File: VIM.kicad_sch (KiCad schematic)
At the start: 13 parts, among them U3 INA139, U4 MAX11615, U5 INA139

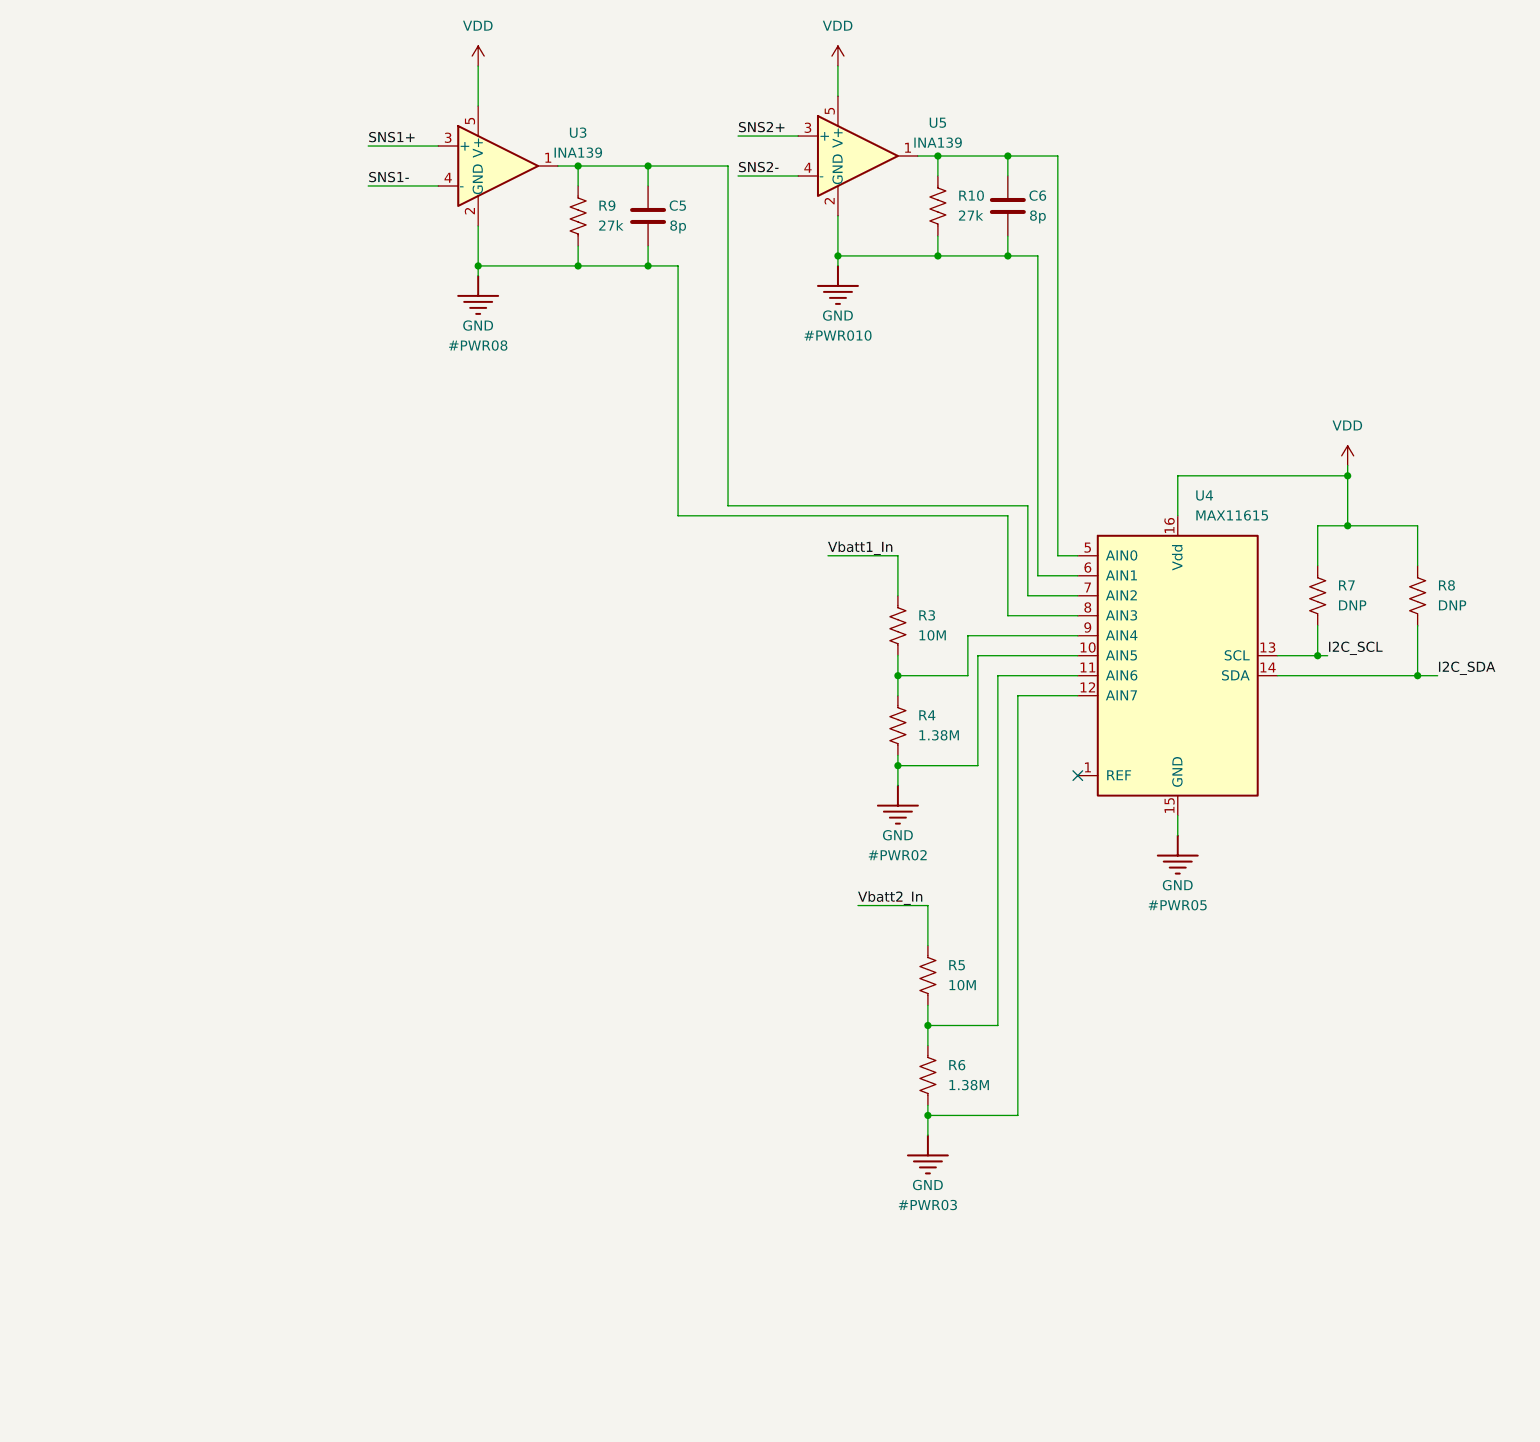
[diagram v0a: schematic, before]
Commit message: Added some ports
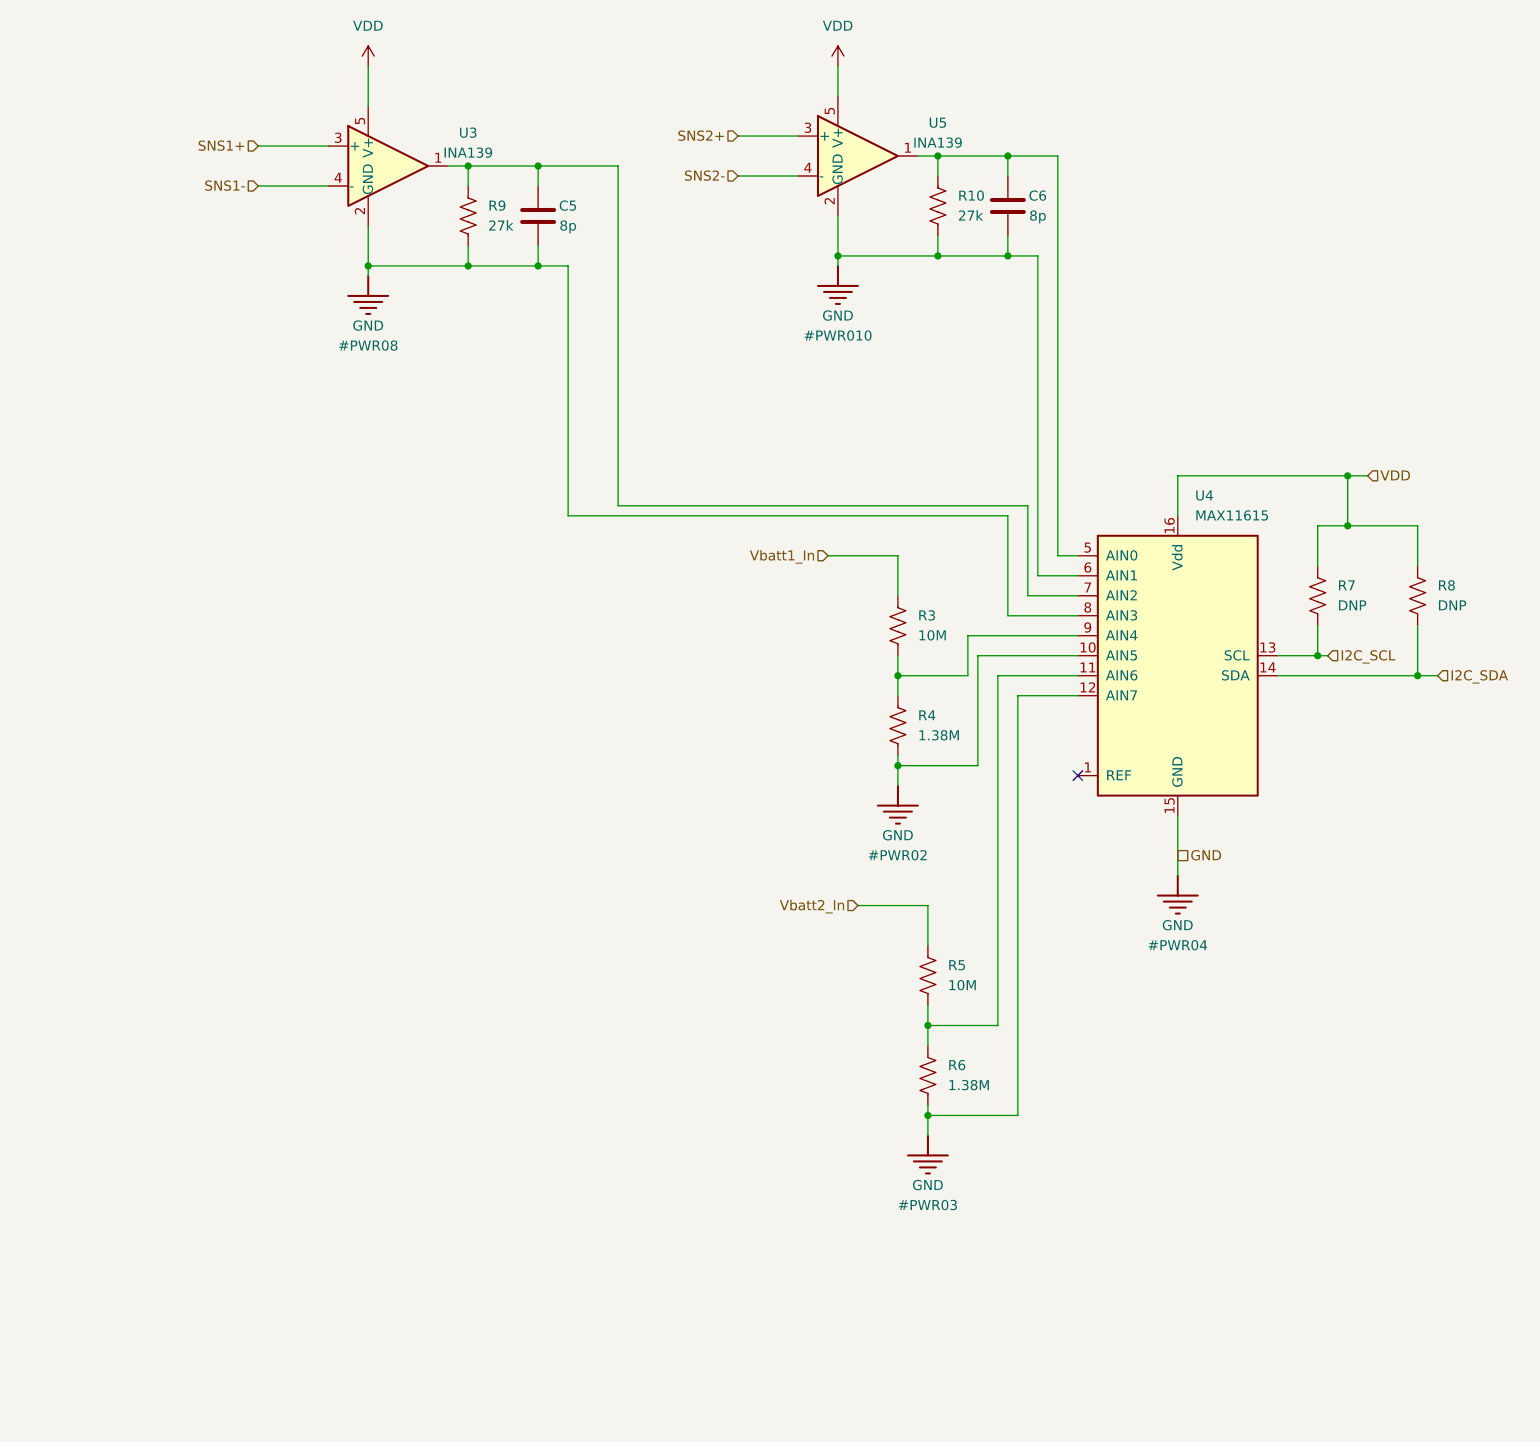
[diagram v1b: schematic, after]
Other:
- moved on the sheet: C5, R9, U3

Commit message: added rc lp and cm filter to vdiv
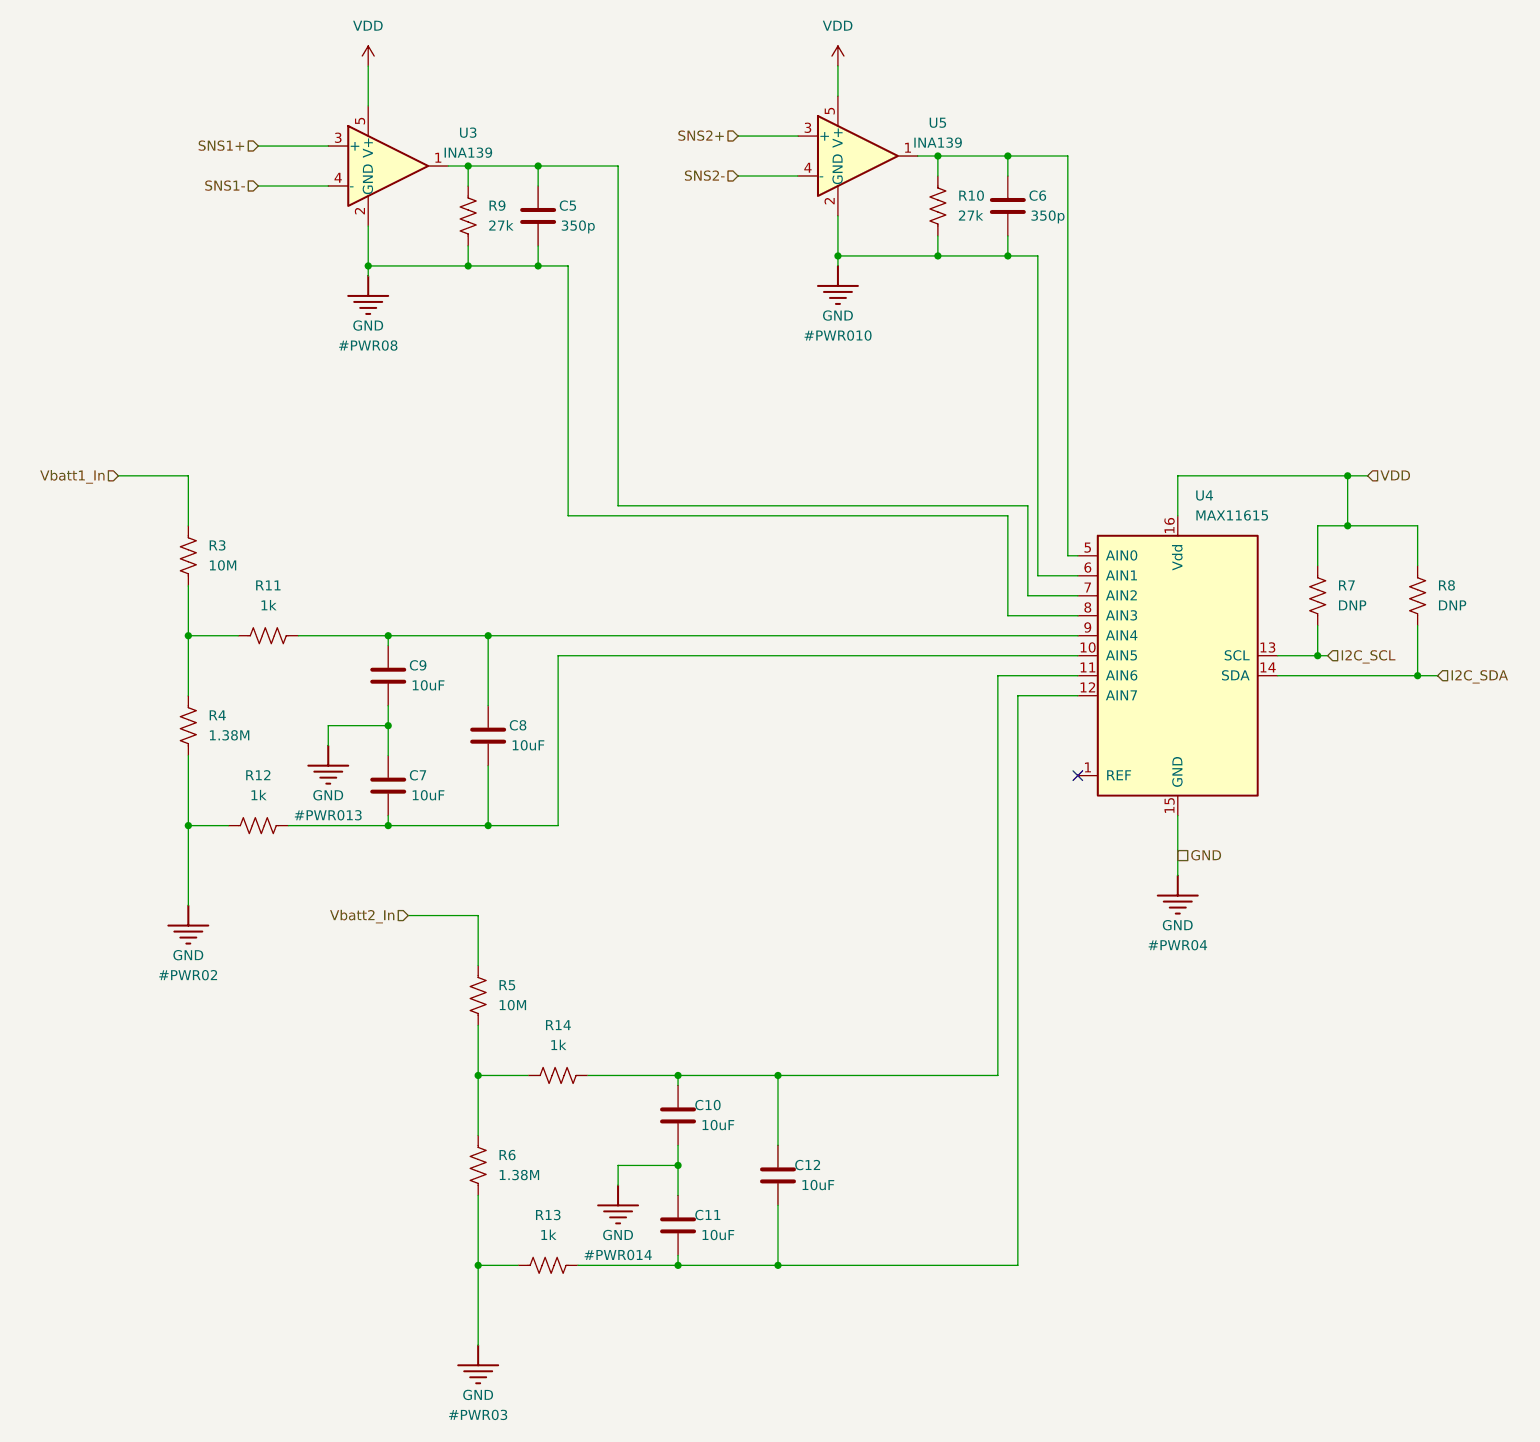
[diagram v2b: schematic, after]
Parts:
- added C10, C11, C12, C7, C8, C9: 10uF, Capacitor_SMD:C_0805_2012Metric_Pad1.18x1.45mm_HandSolder, symbol Device:C
- added R11, R12, R13, R14: 1k, Resistor_SMD:R_0805_2012Metric_Pad1.20x1.40mm_HandSolder, symbol Device:R_US
- C5, C6: value 8p -> 350p
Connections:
- net GND: now also C10.1, C11.2, C7.2, C9.1, R12.2, R13.2; no longer U4.10 (AIN5), U4.12 (AIN7)
- net at R5.1, R6.1: now also R14.2; no longer U4.11 (AIN6)
- net at R3.1, R4.1: now also R11.2; no longer U4.9 (AIN4)
- new net: C10.2, C12.2, R14.1, U4.11 (AIN6)
- new net: C8.2, C9.2, R11.1, U4.9 (AIN4)
- new net: C11.1, C12.1, R13.1, U4.12 (AIN7)
- new net: C7.1, C8.1, R12.1, U4.10 (AIN5)
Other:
- moved on the sheet: R3, R4

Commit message: changed circuit
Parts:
- removed C11, C12, C7, C8: 10uF, Capacitor_SMD:C_0805_2012Metric_Pad1.18x1.45mm_HandSolder, symbol Device:C
- removed R12, R13: 1k, Resistor_SMD:R_0805_2012Metric_Pad1.20x1.40mm_HandSolder, symbol Device:R_US
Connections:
- net GND: now also U4.10 (AIN5), U4.12 (AIN7)
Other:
- moved on the sheet: C10, C9

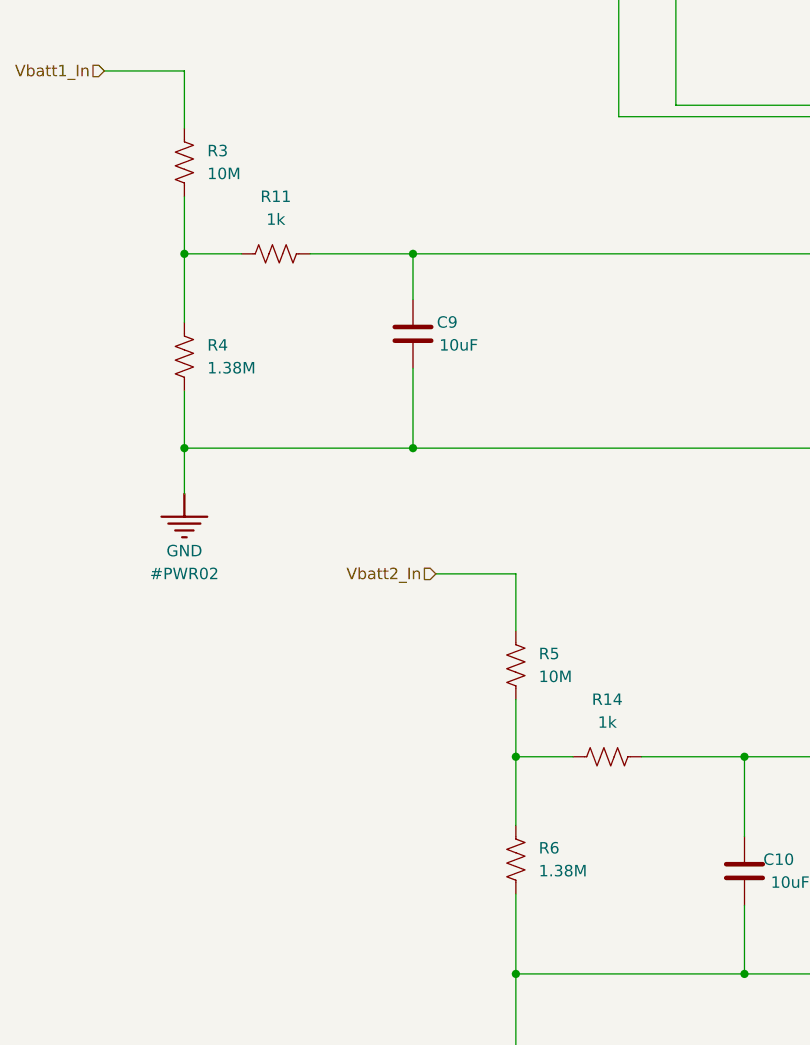
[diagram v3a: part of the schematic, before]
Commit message: changed v-divider
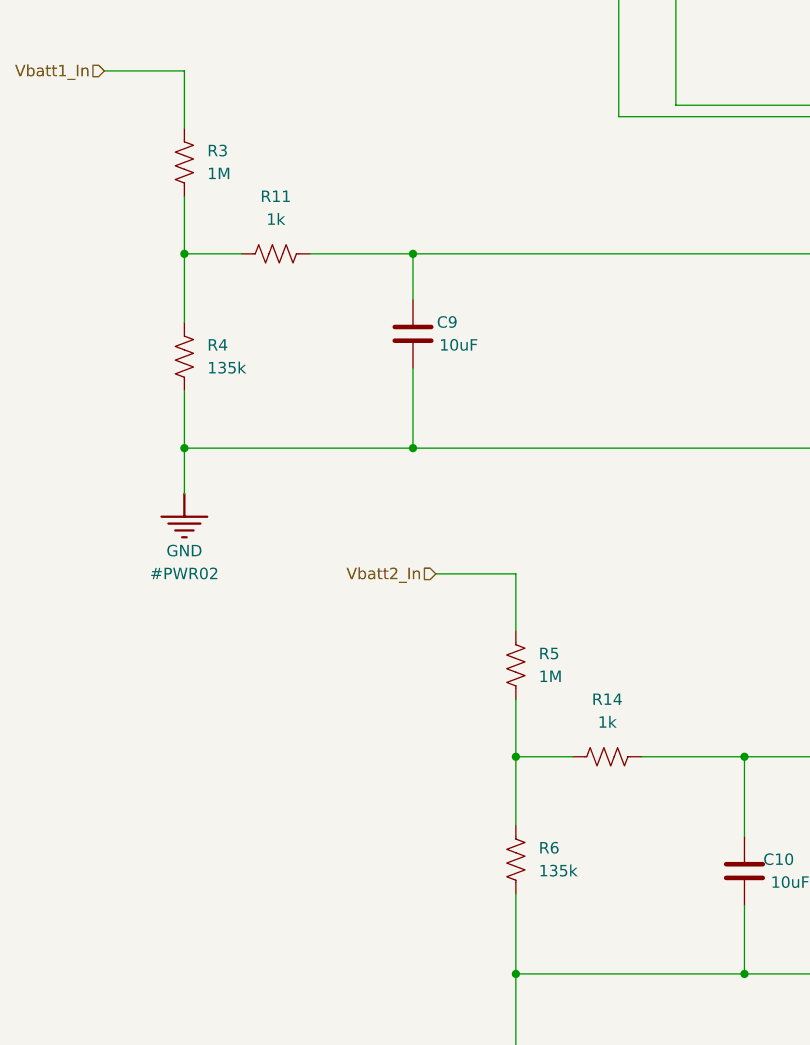
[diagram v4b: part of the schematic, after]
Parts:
- R3, R5: value 10M -> 1M
- R4, R6: value 1.38M -> 135k
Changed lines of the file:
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@@
       (effects (font (size 1.27 1.27)) (justify left))
     )
-    (property "Value" "1.38M" (at 85.09 172.72 0)
+    (property "Value" "135k" (at 85.09 172.72 0)
       (effects (font (size 1.27 1.27)) (justify left))
     )
@@
       (effects (font (size 1.27 1.27)) (justify right))
     )
-    (property "Value" "10M" (at 85.09 151.13 0)
+    (property "Value" "1M" (at 85.09 151.13 0)
       (effects (font (size 1.27 1.27)) (justify right))
     )
@@
       (effects (font (size 1.27 1.27)) (justify right))
     )
-    (property "Value" "10M" (at 48.26 95.25 0)
+    (property "Value" "1M" (at 48.26 95.25 0)
       (effects (font (size 1.27 1.27)) (justify right))
     )
@@
       (effects (font (size 1.27 1.27)) (justify left))
     )
-    (property "Value" "1.38M" (at 48.26 116.84 0)
-      (effects (font (size 1.27 1.27)) (justify left))
-    )
+    (property "Value" "135k" (at 48.26 116.84 0)
+      (effects (font (size 1.27 1.27)) (justify left))
+    )

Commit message: contemplated life and then changed it again
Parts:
- R4, R6: value 135k -> 127k
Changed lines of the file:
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@@
       (effects (font (size 1.27 1.27)) (justify left))
     )
-    (property "Value" "135k" (at 85.09 172.72 0)
+    (property "Value" "127k" (at 85.09 172.72 0)
       (effects (font (size 1.27 1.27)) (justify left))
     )
@@
       (effects (font (size 1.27 1.27)) (justify left))
     )
-    (property "Value" "135k" (at 48.26 116.84 0)
-      (effects (font (size 1.27 1.27)) (justify left))
-    )
+    (property "Value" "127k" (at 48.26 116.84 0)
+      (effects (font (size 1.27 1.27)) (justify left))
+    )
